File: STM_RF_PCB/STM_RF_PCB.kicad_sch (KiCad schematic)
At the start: 46 parts, among them J1 SMA, J2 USB_B_Micro, J3 SWD STLINk, J4 Conn_01x04, SW1 UP, SW2 LF, SW3 DN, SW4 RT, SW5 A, SW6 B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

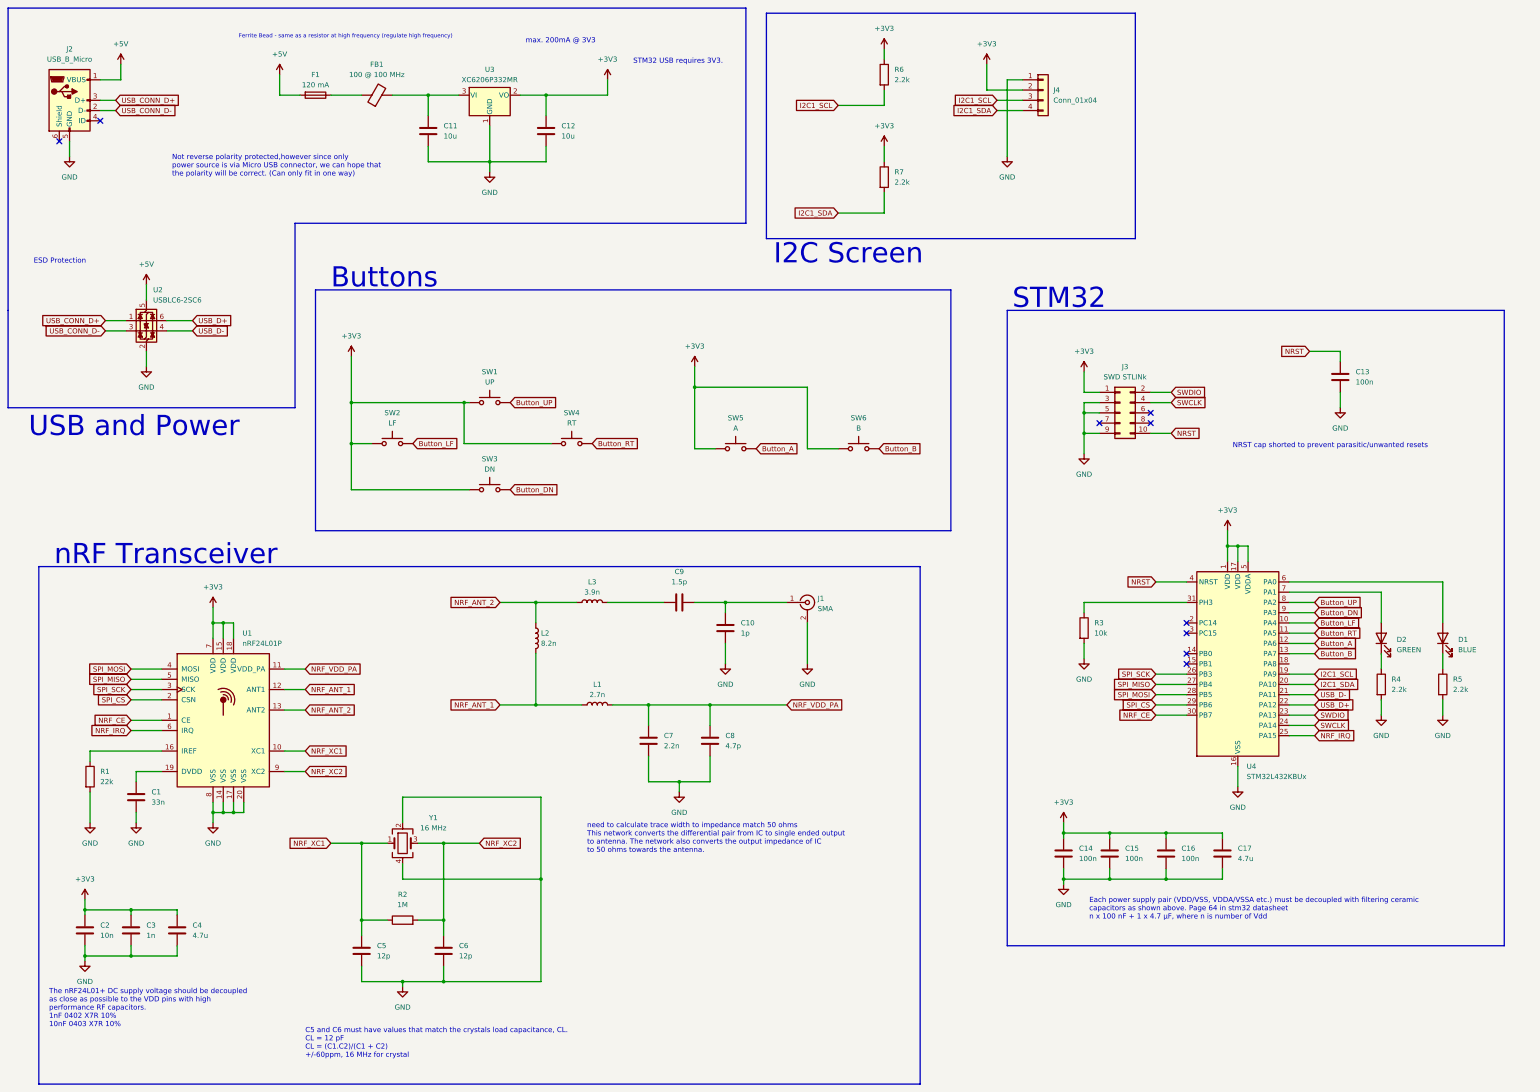
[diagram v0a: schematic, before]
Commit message: Added start select buttons
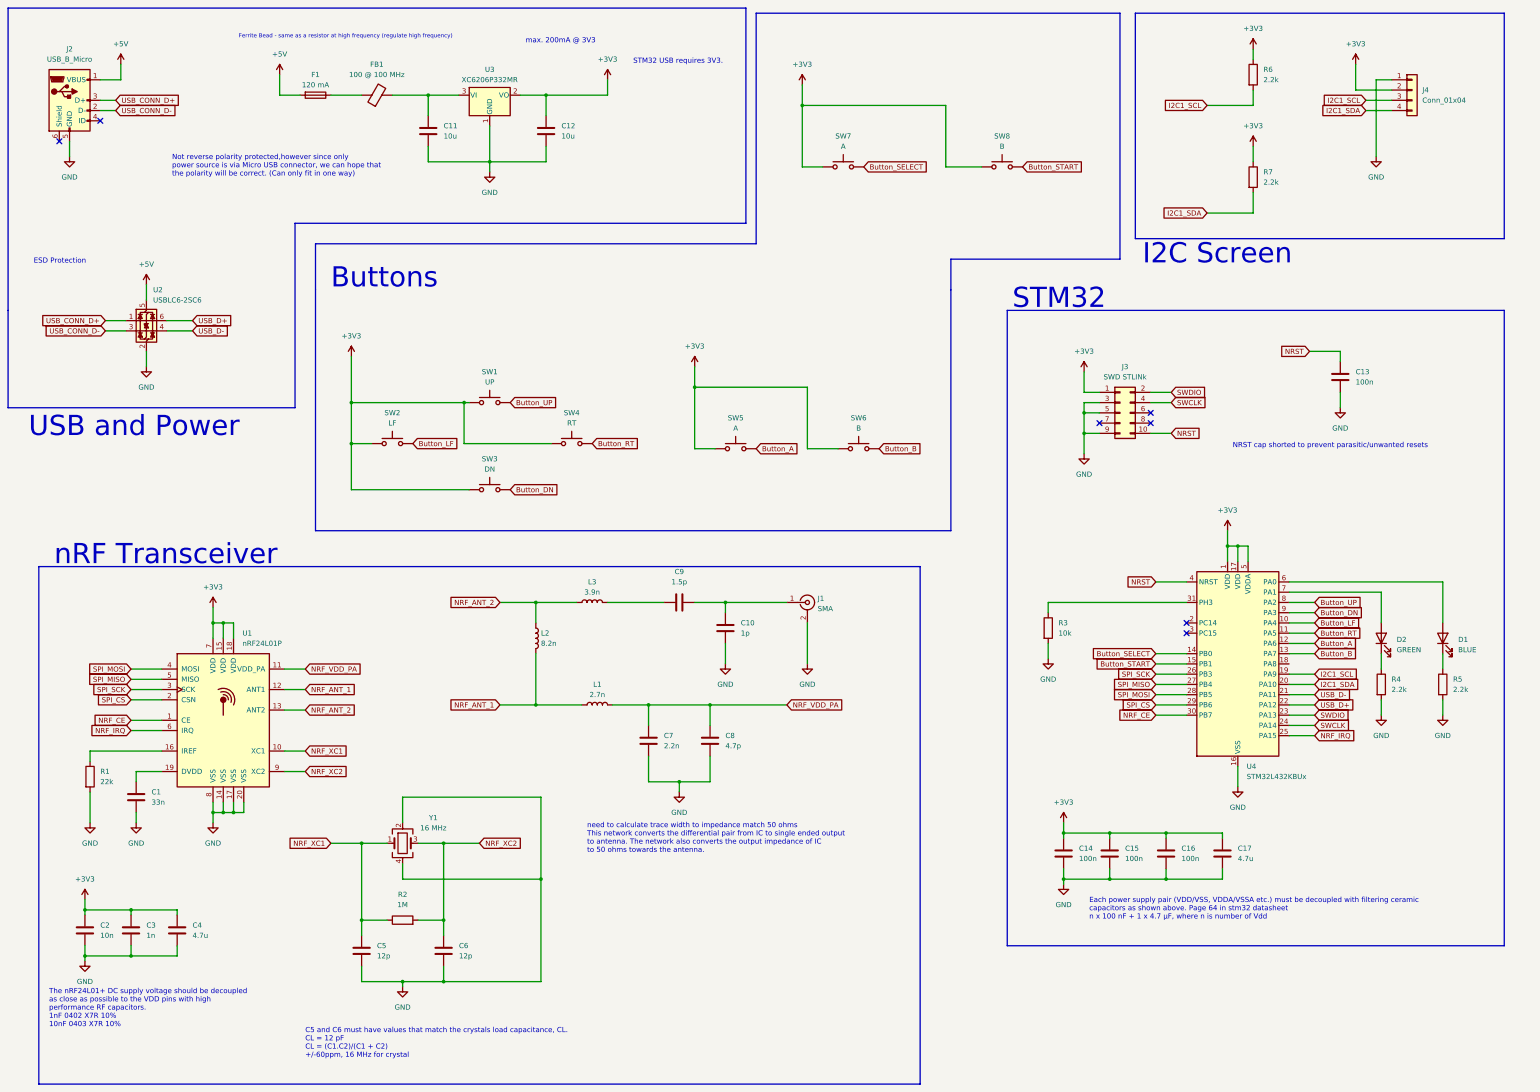
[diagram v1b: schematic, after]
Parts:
- added SW7: A, Library:TC-1103-C-D, symbol Switch:SW_Push
- added SW8: B, Library:TC-1103-C-D, symbol Switch:SW_Push
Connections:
- net +3V3: now also SW7.1, SW8.1
- net Button_SELECT: now reaches U4.14 (PB0)
- net Button_SELECT: now also SW7.2
- net Button_START: now reaches U4.15 (PB1)
- net Button_START: now also SW8.2
- no-connect marks 9 -> 7
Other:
- moved on the sheet: J4, R3, R6, R7

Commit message: PCB work
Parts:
- SW7: value A -> SELECT
- SW8: value B -> START
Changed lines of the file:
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@@
 			)
 		)
-		(property "Value" "B"
+		(property "Value" "START"
 			(at 259.08 48.26 0)
 			(effects
@@
 			)
 		)
-		(property "Value" "A"
+		(property "Value" "SELECT"
 			(at 219.71 48.26 0)
 			(effects

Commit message: PCB work
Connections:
- no-connect marks 7 -> 9
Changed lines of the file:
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@@
+	)
+	(no_connect
+		(at 342.9 161.29)
 	)
 	(no_connect
@@
 	)
 	(no_connect
+		(at 330.2 176.53)
+	)
+	(no_connect

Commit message: PCB work
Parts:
- U3: footprint Package_TO_SOT_SMD:SOT-23-3 -> Library:XC6206P332MR
- U4: value STM32L432KBUx -> STM32L432KBU6; footprint Package_DFN_QFN:UFQFPN-32-1EP_5x5mm_P0.5mm_EP3.5x3.5mm -> Library:STM32L432KBU6
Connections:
- net Button_LF: now also U4.11 (PA5); no longer U4.10 (PA4)
- net Button_RT: now also U4.10 (PA4); no longer U4.11 (PA5)
- no-connect marks 9 -> 8
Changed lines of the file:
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@@
 	)
 	(no_connect
-		(at 342.9 161.29)
-	)
-	(no_connect
 		(at 283.21 116.84)
 	)
@@
 	(wire
 		(pts
+			(xy 330.2 168.91) (xy 336.55 168.91)
+		)
+		(stroke
+			(width 0)
+			(type default)
+		)
+	)
+	(wire
+		(pts
 			(xy 66.04 170.18) (xy 66.04 166.37)
 		)
@@
 	(wire
 		(pts
-			(xy 330.2 166.37) (xy 336.55 166.37)
-		)
-		(stroke
-			(width 0)
-			(type default)
-		)
-	)
-	(wire
-		(pts
 			(xy 330.2 171.45) (xy 336.55 171.45)
 		)
@@
 	(wire
 		(pts
+			(xy 330.2 166.37) (xy 336.55 166.37)
+		)
+		(stroke
+			(width 0)
+			(type default)
+		)
+	)
+	(wire
+		(pts
 			(xy 110.49 215.9) (xy 110.49 209.55)
 		)
@@
 	(wire
 		(pts
-			(xy 330.2 168.91) (xy 336.55 168.91)
-		)
-		(stroke
-			(width 0)
-			(type default)
-		)
-	)
-	(wire
-		(pts
 			(xy 54.61 246.38) (xy 54.61 248.92)
 		)
@@
 	(global_label "Button_RT"
 		(shape input)
-		(at 336.55 168.91 0)
+		(at 336.55 166.37 0)
 		(fields_autoplaced yes)
 		(effects
@@
 		)
 		(property "Intersheetrefs" "${INTERSHEET_REFS}"
-			(at 348.9088 168.91 0)
+			(at 348.9088 166.37 0)
 			(effects
 				(font
@@
 	(global_label "Button_LF"
 		(shape input)
-		(at 336.55 166.37 0)
+		(at 336.55 168.91 0)
 		(fields_autoplaced yes)
 		(effects
@@
 		)
 		(property "Intersheetrefs" "${INTERSHEET_REFS}"
-			(at 348.7879 166.37 0)
+			(at 348.7879 168.91 0)
 			(effects
 				(font
@@
 			)
 		)
-		(property "Value" "STM32L432KBUx"
+		(property "Value" "STM32L432KBU6"
 			(at 319.6941 204.47 0)
 			(effects
@@
 			)
 		)
-		(property "Footprint" "Package_DFN_QFN:UFQFPN-32-1EP_5x5mm_P0.5mm_EP3.5x3.5mm"
+		(property "Footprint" "Library:STM32L432KBU6"
 			(at 307.34 199.39 0)
 			(effects
@@
 			)
 		)
-		(property "Footprint" "Package_TO_SOT_SMD:SOT-23-3"
+		(property "Footprint" "Library:XC6206P332MR"
 			(at 132.08 29.845 0)
 			(effects

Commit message: pcb work
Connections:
- net USB_CONN_D+: now also U2.3 (I/O2); no longer U2.1 (I/O1)
- net USB_CONN_D-: now also U2.1 (I/O1); no longer U2.3 (I/O2)
- net USB_D+: now also U2.4 (I/O2); no longer U2.6 (I/O1)
- net USB_D-: now also U2.6 (I/O1); no longer U2.4 (I/O2)
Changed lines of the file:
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@@
 	(wire
 		(pts
+			(xy 52.07 91.44) (xy 58.42 91.44)
+		)
+		(stroke
+			(width 0)
+			(type default)
+		)
+	)
+	(wire
+		(pts
 			(xy 116.84 48.26) (xy 116.84 52.07)
 		)
@@
 	(wire
 		(pts
-			(xy 52.07 91.44) (xy 58.42 91.44)
-		)
-		(stroke
-			(width 0)
-			(type default)
-		)
-	)
-	(wire
-		(pts
 			(xy 54.61 237.49) (xy 43.18 237.49)
 		)
@@
 	(wire
 		(pts
+			(xy 36.83 93.98) (xy 41.91 93.98)
+		)
+		(stroke
+			(width 0)
+			(type default)
+		)
+	)
+	(wire
+		(pts
 			(xy 297.18 184.15) (xy 304.8 184.15)
 		)
@@
 	(wire
 		(pts
+			(xy 36.83 91.44) (xy 41.91 91.44)
+		)
+		(stroke
+			(width 0)
+			(type default)
+		)
+	)
+	(wire
+		(pts
 			(xy 330.2 168.91) (xy 336.55 168.91)
 		)
@@
 	(wire
 		(pts
-			(xy 342.9 101.6) (xy 342.9 99.06)
+			(xy 52.07 93.98) (xy 58.42 93.98)
 		)
 		(stroke
@@
 	(wire
 		(pts
-			(xy 314.96 147.32) (xy 314.96 151.13)
+			(xy 342.9 101.6) (xy 342.9 99.06)
 		)
 		(stroke
@@
 	(wire
 		(pts
-			(xy 36.83 91.44) (xy 41.91 91.44)
+			(xy 314.96 147.32) (xy 314.96 151.13)
 		)
 		(stroke
@@
 		)
 	)
-	(wire
-		(pts
-			(xy 52.07 93.98) (xy 58.42 93.98)
-		)
-		(stroke
-			(width 0)
-			(type default)
-		)
-	)
 	(polyline
 		(pts
@@
 	(wire
 		(pts
-			(xy 36.83 93.98) (xy 41.91 93.98)
-		)
-		(stroke
-			(width 0)
-			(type default)
-		)
-	)
-	(wire
-		(pts
 			(xy 349.25 36.83) (xy 355.6 36.83)
 		)
@@
 	(global_label "USB_D-"
 		(shape input)
-		(at 58.42 93.98 0)
+		(at 58.42 91.44 0)
 		(fields_autoplaced yes)
 		(effects
@@
 		)
 		(property "Intersheetrefs" "${INTERSHEET_REFS}"
-			(at 69.0252 93.98 0)
+			(at 69.0252 91.44 0)
 			(effects
 				(font
@@
 	(global_label "USB_CONN_D-"
 		(shape input)
-		(at 36.83 93.98 180)
+		(at 36.83 91.44 180)
 		(fields_autoplaced yes)
 		(effects
@@
 		)
 		(property "Intersheetrefs" "${INTERSHEET_REFS}"
-			(at 19.9957 93.98 0)
+			(at 19.9957 91.44 0)
 			(effects
 				(font
@@
 	(global_label "USB_D+"
 		(shape input)
-		(at 58.42 91.44 0)
+		(at 58.42 93.98 0)
 		(fields_autoplaced yes)
 		(effects
@@
 		)
 		(property "Intersheetrefs" "${INTERSHEET_REFS}"
-			(at 69.0252 91.44 0)
+			(at 69.0252 93.98 0)
 			(effects
 				(font
@@
 	(global_label "USB_CONN_D+"
 		(shape input)
-		(at 36.83 91.44 180)
+		(at 36.83 93.98 180)
 		(fields_autoplaced yes)
 		(effects
@@
 		)
 		(property "Intersheetrefs" "${INTERSHEET_REFS}"
-			(at 19.9957 91.44 0)
+			(at 19.9957 93.98 0)
 			(effects
 				(font

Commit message: Fab outputs
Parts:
- C2: Part ID CL10A106KP8NNNC -> 0603B103K101NT
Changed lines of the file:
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@@
 			)
 		)
-		(property "Part ID" "CL10A106KP8NNNC"
+		(property "Part ID" "0603B103K101NT"
 			(at 31.75 242.57 0)
 			(effects
